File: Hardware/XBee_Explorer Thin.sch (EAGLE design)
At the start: 64 parts, among them J4 QWIIC_RIGHT_ANGLE, Q2 3.1A/30V/105mΩ, U1 FSUSB30MUX_MSOP10, U2 AP63203, U3 ESD Diode, U5 ESD Diode, U6 CP210X

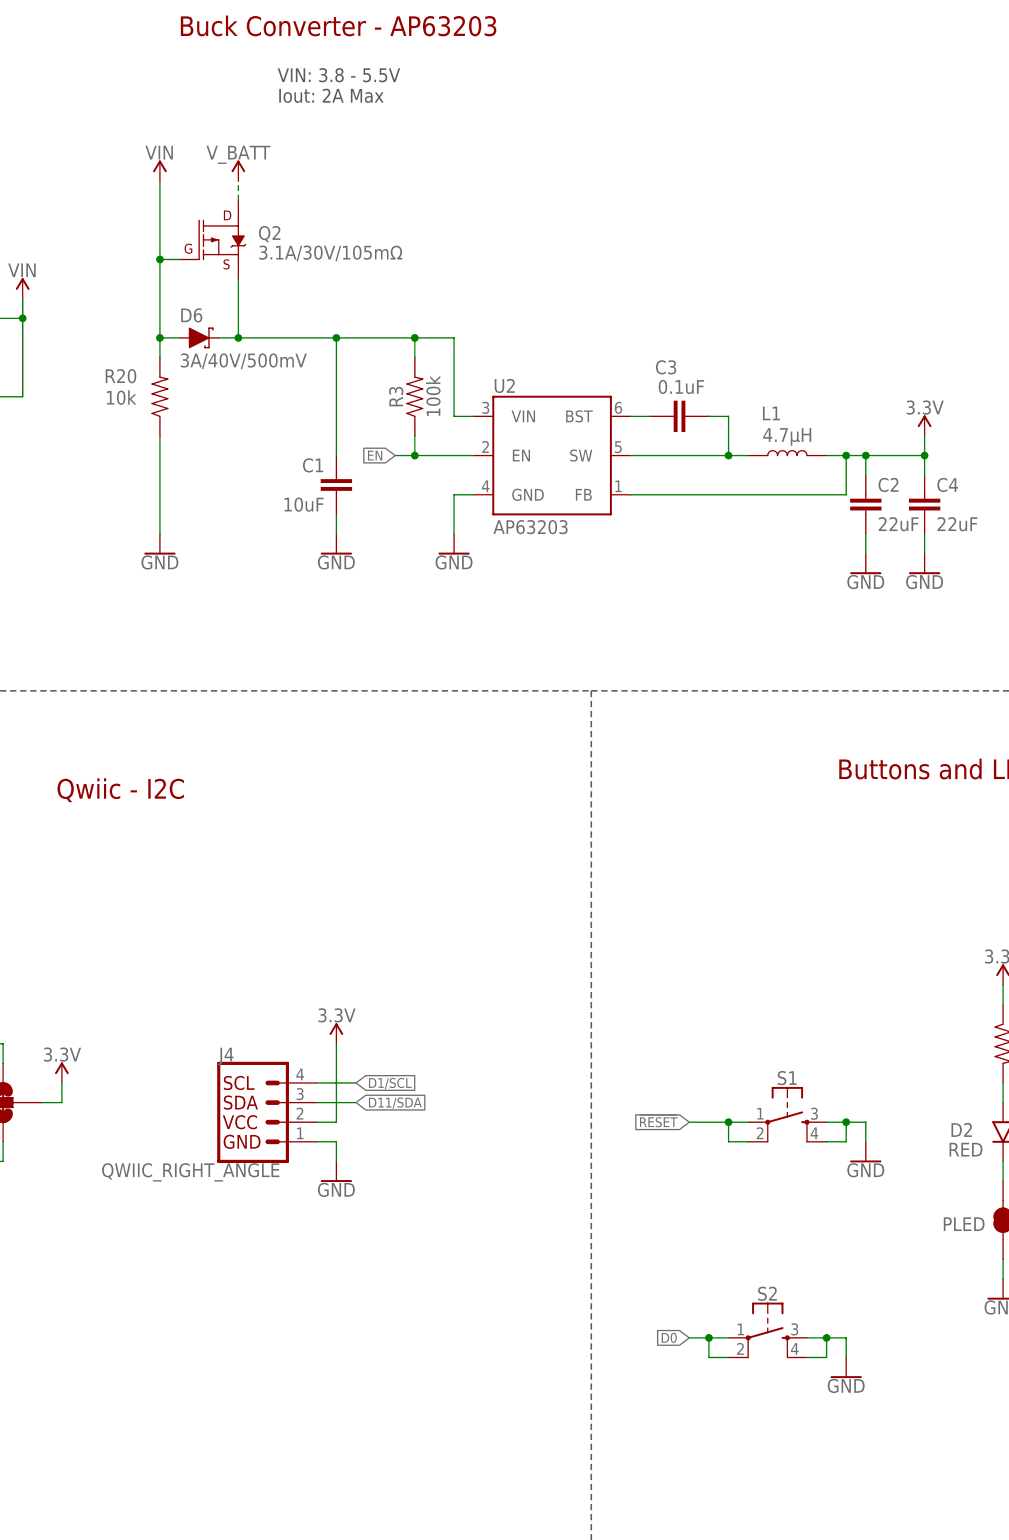
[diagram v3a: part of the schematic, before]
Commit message: Replaces the only 0402 on the board with an 0603, replaces only 100k resistor with a 10k, fixes input/ouput labeling
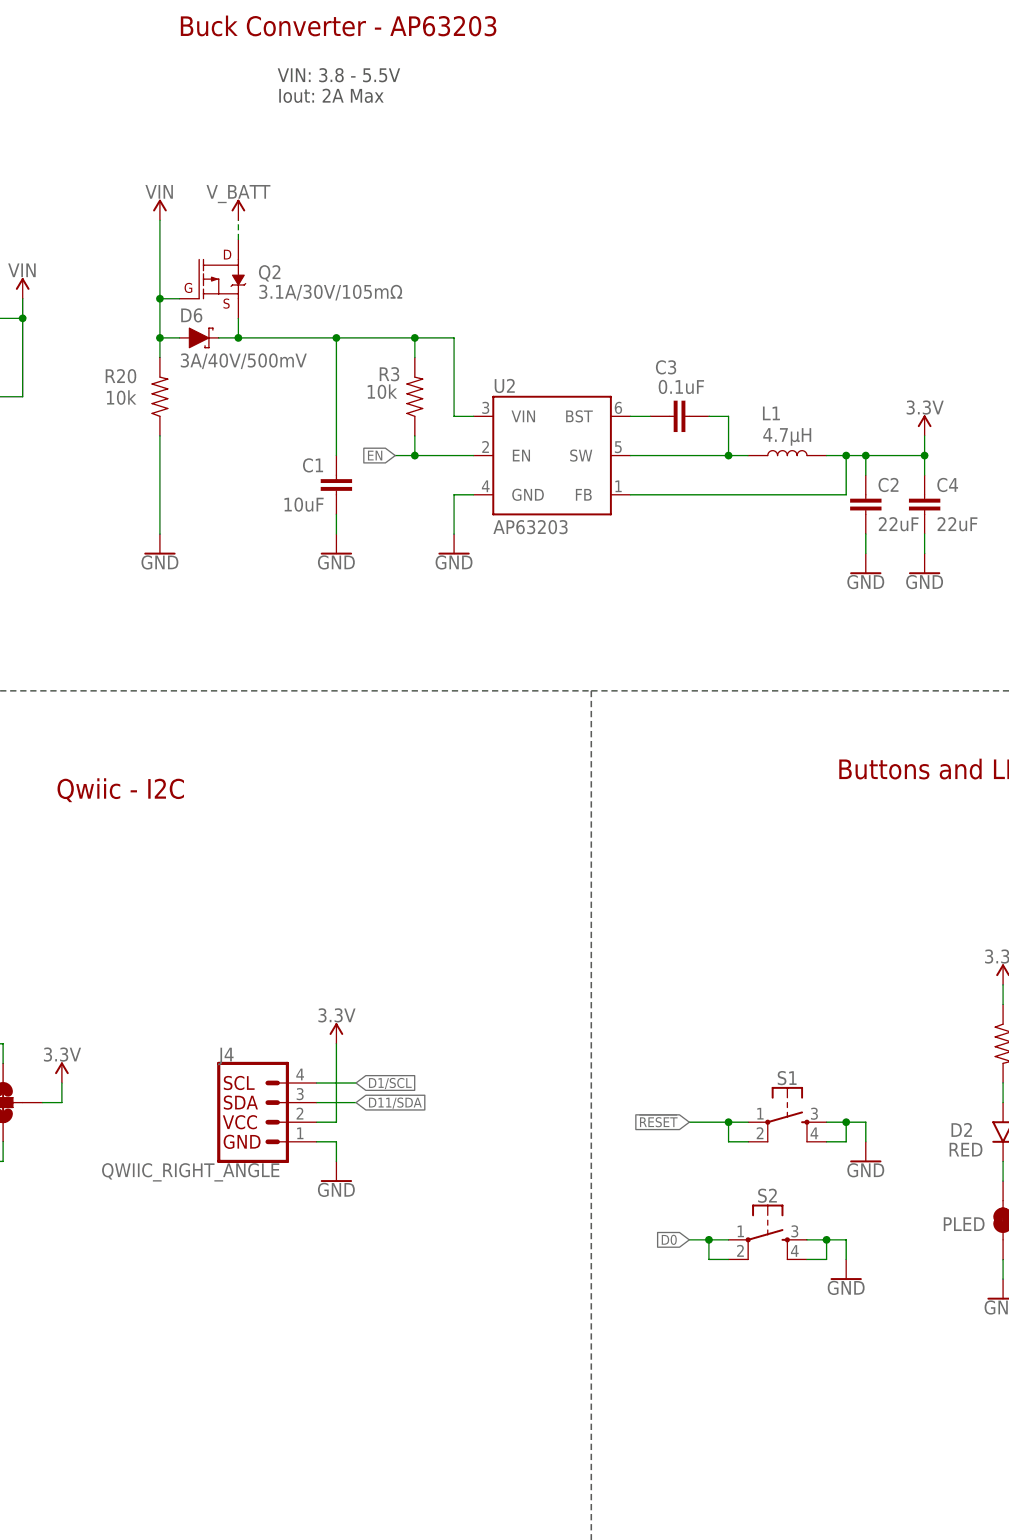
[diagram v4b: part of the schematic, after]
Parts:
- C6: device SparkFun-Capacitors:10NF-0402T-25V-10% -> SparkFun-Capacitors:10NF-0603-50V-10%
- R3: value 100k -> 10k; device SparkFun-Resistors:100KOHM-0603-1/10W-1% -> SparkFun-Resistors:10KOHM-0603-1/10W-1%
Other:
- moved on the sheet: Q2, S2
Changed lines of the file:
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@@
 <part name="SUPPLY7" library="SparkFun-PowerSymbols" deviceset="3.3V" device=""/>
 <part name="C1" library="SparkFun-Capacitors" deviceset="10UF" device="-1210-50V-20%" value="10uF"/>
-<part name="R3" library="SparkFun-Resistors" deviceset="100KOHM" device="-0603-1/10W-1%" value="100k"/>
+<part name="R3" library="SparkFun-Resistors" deviceset="10KOHM" device="-0603-1/10W-1%" value="10k"/>
 <part name="GND3" library="SparkFun-PowerSymbols" deviceset="GND" device=""/>
 <part name="GND21" library="SparkFun-PowerSymbols" deviceset="GND" device=""/>
@@
 <part name="GND33" library="SparkFun-PowerSymbols" deviceset="GND" device=""/>
 <part name="GND34" library="SparkFun-PowerSymbols" deviceset="GND" device=""/>
-<part name="C6" library="SparkFun-Capacitors" deviceset="10NF" device="-0402T-25V-10%" value="10nF"/>
+<part name="C6" library="SparkFun-Capacitors" deviceset="10NF" device="-0603-50V-10%" value="10nF"/>
 <part name="C7" library="SparkFun-Capacitors" deviceset="10NF" device="-0603-50V-10%" value="10nF"/>
 <part name="C9" library="SparkFun-Capacitors" deviceset="0.1UF" device="-0603-25V-(+80/-20%)" value="0.1uF"/>
@@
 <attribute name="VALUE" x="271.78" y="50.546" size="1.778" layer="96" font="vector" align="top-center"/>
 </instance>
-<instance part="S2" gate="G$1" x="259.08" y="27.94" smashed="yes">
-<attribute name="NAME" x="259.08" y="32.766" size="1.778" layer="95" font="vector" align="bottom-center"/>
-<attribute name="VALUE" x="259.08" y="25.146" size="1.778" layer="96" font="vector" align="top-center"/>
-</instance>
-<instance part="GND2" gate="1" x="269.24" y="22.86" smashed="yes">
-<attribute name="VALUE" x="269.24" y="22.606" size="1.778" layer="96" font="vector" align="top-center"/>
+<instance part="S2" gate="G$1" x="259.08" y="40.64" smashed="yes">
+<attribute name="NAME" x="259.08" y="45.466" size="1.778" layer="95" font="vector" align="bottom-center"/>
+<attribute name="VALUE" x="259.08" y="37.846" size="1.778" layer="96" font="vector" align="top-center"/>
+</instance>
+<instance part="GND2" gate="1" x="269.24" y="35.56" smashed="yes">
+<attribute name="VALUE" x="269.24" y="35.306" size="1.778" layer="96" font="vector" align="top-center"/>
 </instance>
 <instance part="J5" gate="J1" x="91.44" y="142.24" smashed="yes" rot="R180">
@@
 <attribute name="VALUE" x="71.12" y="71.374" size="1.778" layer="96" font="vector" rot="MR0" align="bottom-center"/>
 </instance>
-<instance part="SUPPLY17" gate="G$1" x="190.5" y="177.8" smashed="yes">
-<attribute name="VALUE" x="190.5" y="180.594" size="1.778" layer="96" font="vector" align="bottom-center"/>
+<instance part="SUPPLY17" gate="G$1" x="190.5" y="172.72" smashed="yes">
+<attribute name="VALUE" x="190.5" y="175.514" size="1.778" layer="96" font="vector" align="bottom-center"/>
 </instance>
 <instance part="D6" gate="G$1" x="185.42" y="157.48" smashed="yes">
@@
 <attribute name="VALUE" x="182.88" y="155.448" size="1.778" layer="96" font="vector" align="top-left"/>
 </instance>
-<instance part="Q2" gate="G$1" x="187.96" y="170.18" smashed="yes">
-<attribute name="NAME" x="193.04" y="170.18" size="1.778" layer="95" font="vector"/>
-<attribute name="VALUE" x="193.04" y="167.64" size="1.778" layer="96" font="vector"/>
+<instance part="Q2" gate="G$1" x="187.96" y="165.1" smashed="yes">
+<attribute name="NAME" x="193.04" y="165.1" size="1.778" layer="95" font="vector"/>
+<attribute name="VALUE" x="193.04" y="162.56" size="1.778" layer="96" font="vector"/>
 </instance>
 <instance part="R20" gate="G$1" x="180.34" y="149.86" smashed="yes" rot="R90">
@@
 <attribute name="VALUE" x="137.16" y="155.194" size="1.778" layer="96" font="vector" align="bottom-center"/>
 </instance>
-<instance part="SUPPLY5" gate="G$1" x="180.34" y="177.8" smashed="yes">
-<attribute name="VALUE" x="180.34" y="180.594" size="1.778" layer="96" font="vector" align="bottom-center"/>
+<instance part="SUPPLY5" gate="G$1" x="180.34" y="172.72" smashed="yes">
+<attribute name="VALUE" x="180.34" y="175.514" size="1.778" layer="96" font="vector" align="bottom-center"/>
 </instance>
 <instance part="SUPPLY15" gate="G$1" x="162.56" y="162.56" smashed="yes">
@@
 </instance>
 <instance part="R3" gate="G$1" x="213.36" y="149.86" smashed="yes" rot="R90">
-<attribute name="NAME" x="211.836" y="149.86" size="1.778" layer="95" font="vector" rot="R90" align="bottom-center"/>
-<attribute name="VALUE" x="214.884" y="149.86" size="1.778" layer="96" font="vector" rot="R90" align="top-center"/>
+<attribute name="NAME" x="210.058" y="153.67" size="1.778" layer="95" font="vector" rot="R180" align="bottom-center"/>
+<attribute name="VALUE" x="209.042" y="149.606" size="1.778" layer="96" font="vector" rot="R180" align="top-center"/>
 </instance>
 <instance part="GND3" gate="1" x="203.2" y="129.54" smashed="yes">
@@
 <segment>
 <pinref part="S2" gate="G$1" pin="3"/>
-<wire x1="264.16" y1="27.94" x2="266.7" y2="27.94" width="0.1524" layer="91"/>
-<wire x1="266.7" y1="27.94" x2="269.24" y2="27.94" width="0.1524" layer="91"/>
-<wire x1="269.24" y1="27.94" x2="269.24" y2="25.4" width="0.1524" layer="91"/>
+<wire x1="264.16" y1="40.64" x2="266.7" y2="40.64" width="0.1524" layer="91"/>
+<wire x1="266.7" y1="40.64" x2="269.24" y2="40.64" width="0.1524" layer="91"/>
+<wire x1="269.24" y1="40.64" x2="269.24" y2="38.1" width="0.1524" layer="91"/>
 <pinref part="S2" gate="G$1" pin="4"/>
-<wire x1="266.7" y1="27.94" x2="266.7" y2="25.4" width="0.1524" layer="91"/>
-<wire x1="266.7" y1="25.4" x2="264.16" y2="25.4" width="0.1524" layer="91"/>
-<junction x="266.7" y="27.94"/>
+<wire x1="266.7" y1="40.64" x2="266.7" y2="38.1" width="0.1524" layer="91"/>
+<wire x1="266.7" y1="38.1" x2="264.16" y2="38.1" width="0.1524" layer="91"/>
+<junction x="266.7" y="40.64"/>
 <pinref part="GND2" gate="1" pin="GND"/>
 </segment>
@@
 <pinref part="Q2" gate="G$1" pin="D"/>
 <pinref part="SUPPLY17" gate="G$1" pin="V_BATT"/>
-<wire x1="190.5" y1="175.26" x2="190.5" y2="177.8" width="0.1524" layer="91" style="dashdot"/>
+<wire x1="190.5" y1="170.18" x2="190.5" y2="172.72" width="0.1524" layer="91" style="dashdot"/>
 </segment>
 </net>
@@
 <segment>
 <pinref part="S2" gate="G$1" pin="1"/>
-<wire x1="254" y1="27.94" x2="251.46" y2="27.94" width="0.1524" layer="91"/>
+<wire x1="254" y1="40.64" x2="251.46" y2="40.64" width="0.1524" layer="91"/>
 <pinref part="S2" gate="G$1" pin="2"/>
-<wire x1="254" y1="25.4" x2="251.46" y2="25.4" width="0.1524" layer="91"/>
-<wire x1="251.46" y1="25.4" x2="251.46" y2="27.94" width="0.1524" layer="91"/>
-<wire x1="251.46" y1="27.94" x2="248.92" y2="27.94" width="0.1524" layer="91"/>
-<junction x="251.46" y="27.94"/>
-<label x="248.92" y="27.94" size="1.27" layer="95" font="vector" rot="R180" xref="yes"/>
+<wire x1="254" y1="38.1" x2="251.46" y2="38.1" width="0.1524" layer="91"/>
+<wire x1="251.46" y1="38.1" x2="251.46" y2="40.64" width="0.1524" layer="91"/>
+<wire x1="251.46" y1="40.64" x2="248.92" y2="40.64" width="0.1524" layer="91"/>
+<junction x="251.46" y="40.64"/>
+<label x="248.92" y="40.64" size="1.27" layer="95" font="vector" rot="R180" xref="yes"/>
 </segment>
 <segment>
@@
 <segment>
 <pinref part="Q2" gate="G$1" pin="S"/>
-<wire x1="190.5" y1="165.1" x2="190.5" y2="157.48" width="0.1524" layer="91"/>
+<wire x1="190.5" y1="160.02" x2="190.5" y2="157.48" width="0.1524" layer="91"/>
 <pinref part="D6" gate="G$1" pin="C"/>
 <wire x1="187.96" y1="157.48" x2="190.5" y2="157.48" width="0.1524" layer="91"/>
@@
 <pinref part="D6" gate="G$1" pin="A"/>
 <pinref part="Q2" gate="G$1" pin="G"/>
-<wire x1="182.88" y1="167.64" x2="180.34" y2="167.64" width="0.1524" layer="91"/>
+<wire x1="182.88" y1="162.56" x2="180.34" y2="162.56" width="0.1524" layer="91"/>
 <wire x1="180.34" y1="154.94" x2="180.34" y2="157.48" width="0.1524" layer="91"/>
-<wire x1="180.34" y1="157.48" x2="180.34" y2="167.64" width="0.1524" layer="91"/>
+<wire x1="180.34" y1="157.48" x2="180.34" y2="162.56" width="0.1524" layer="91"/>
 <wire x1="180.34" y1="157.48" x2="182.88" y2="157.48" width="0.1524" layer="91"/>
 <junction x="180.34" y="157.48"/>
 <pinref part="R20" gate="G$1" pin="2"/>
-<wire x1="180.34" y1="177.8" x2="180.34" y2="167.64" width="0.1524" layer="91"/>
-<junction x="180.34" y="167.64"/>
+<wire x1="180.34" y1="172.72" x2="180.34" y2="162.56" width="0.1524" layer="91"/>
+<junction x="180.34" y="162.56"/>
 <pinref part="SUPPLY5" gate="G$1" pin="VIN"/>
 </segment>

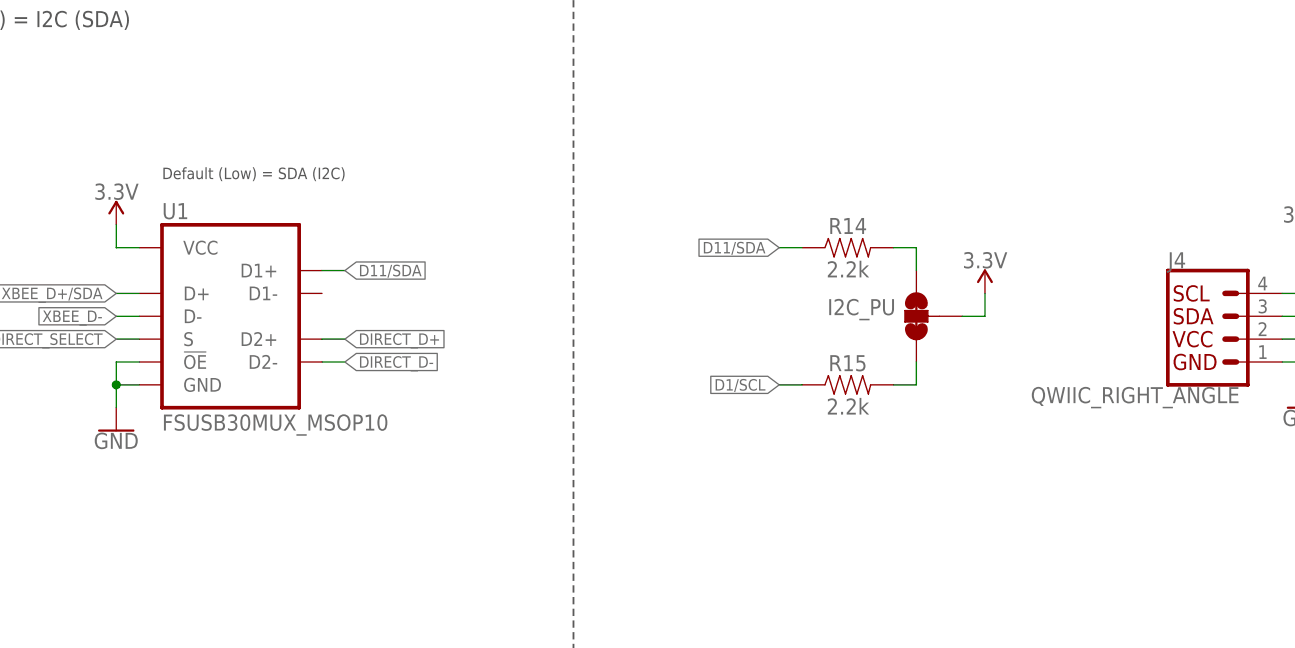
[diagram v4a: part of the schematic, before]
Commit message: Moves resistor colliding with switch, adds via under UART to serial IC, adds "1,2,3,4" in their respective layer
* Moves design to origin
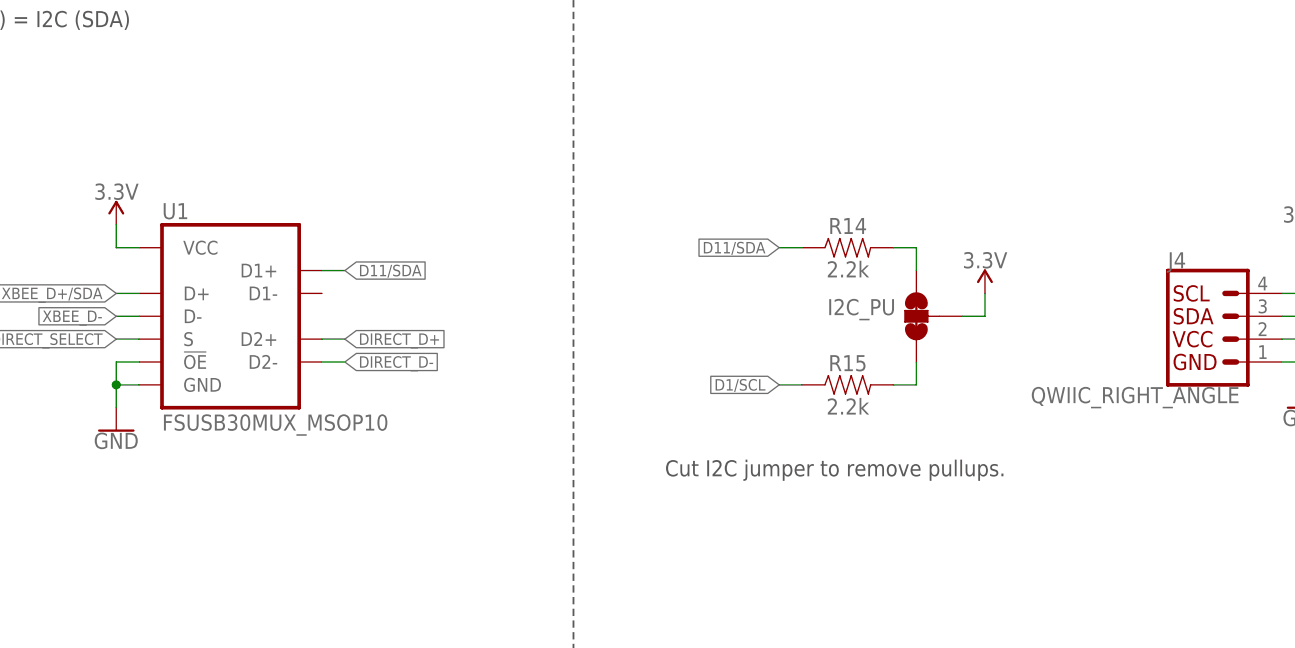
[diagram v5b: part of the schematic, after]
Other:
- note added: "Cut I2C jumper to remove pullups."
- note removed: "Default (Low) = SDA (I2C)"
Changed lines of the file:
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@@
 <text x="424.18" y="7.62" size="2.54" layer="94" font="vector" align="center">v01</text>
 <text x="363.22" y="10.16" size="2.54" layer="94" font="vector" align="center">Elias Santistevan</text>
-<text x="76.2" y="73.66" size="1.27" layer="97" font="vector">Default (Low) = SDA (I2C)</text>
 <wire x1="236.22" y1="111.76" x2="236.22" y2="0" width="0.2032" layer="97" style="longdash"/>
 <text x="58.42" y="99.06" size="2.54" layer="94" font="vector" align="center">USB Switch - FSUSB30</text>
@@
 <text x="200.66" y="269.24" size="2.54" layer="94" font="vector" align="center">USB-C Connectors</text>
 <wire x1="121.92" y1="208.28" x2="294.64" y2="208.28" width="0.1524" layer="97" style="longdash"/>
+<text x="132.08" y="40.64" size="1.778" layer="97" font="vector">Cut I2C jumper to remove pullups.</text>
 </plain>
 <instances>
